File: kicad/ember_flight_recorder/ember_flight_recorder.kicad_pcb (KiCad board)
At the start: 2 copper layers, 25 x 50 mm, 19 parts, among them Q3 FS8205A, Q4 AO3401A, SW1 SW_SPDT, U2 DW01A, U3 MCP1700x-330xxTT, U4 module_mpu6050, U5 module_bme280, U6 ESP32-C3_SUPERMINI_SMD

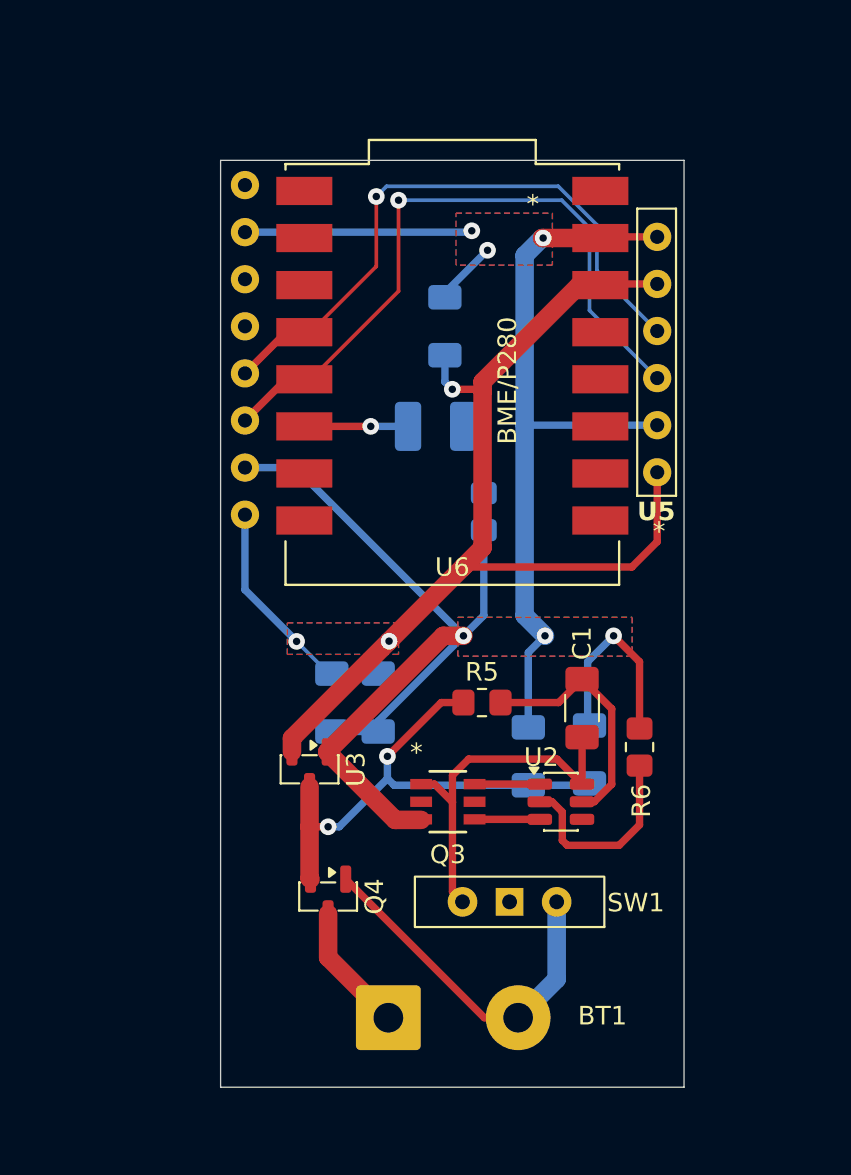
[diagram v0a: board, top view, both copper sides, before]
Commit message: added file logging and http server
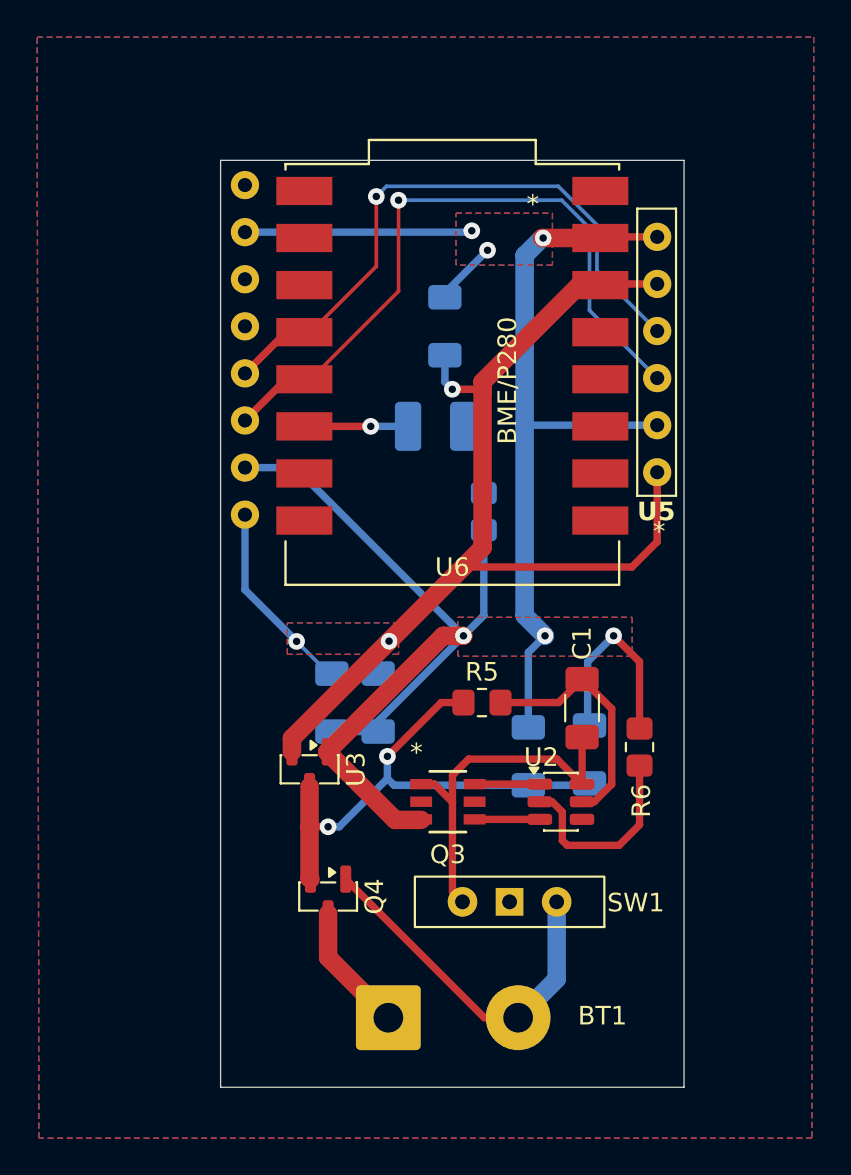
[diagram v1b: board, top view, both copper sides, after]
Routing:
- net VOUT_3V3: track 66.9 -> 69.4 mm
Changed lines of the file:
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@@
+	)
+	(segment
+		(start 136.2 107.9375)
+		(end 138.7 107.9375)
+		(width 0.2)
+		(layer "B.Cu")
+		(net "VOUT_3V3")
 	)
 	(segment
@@
 			)
 		)
+	)
+	(zone
+		(net "GND")
+		(layers "F.Cu" "B.Cu")
+		(name "gnd_pour")
+		(hatch edge 0.5)
+		(priority 2)
+		(connect_pads no
+			(clearance 0.6)
+		)
+		(min_thickness 0.25)
+		(fill yes
+			(thermal_gap 0.5)
+			(thermal_bridge_width 0.5)
+			(island_removal_mode 0)
+		)
+		(polygon
+			(pts
+				(xy 120.3 73.6) (xy 162.2 73.6) (xy 162.1 133) (xy 120.4 133)
+			)
+		)
